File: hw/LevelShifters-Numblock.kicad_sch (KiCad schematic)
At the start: 6 parts, among them U2100 SN74LVCH16T245, U2101 SN74LVCH16T245

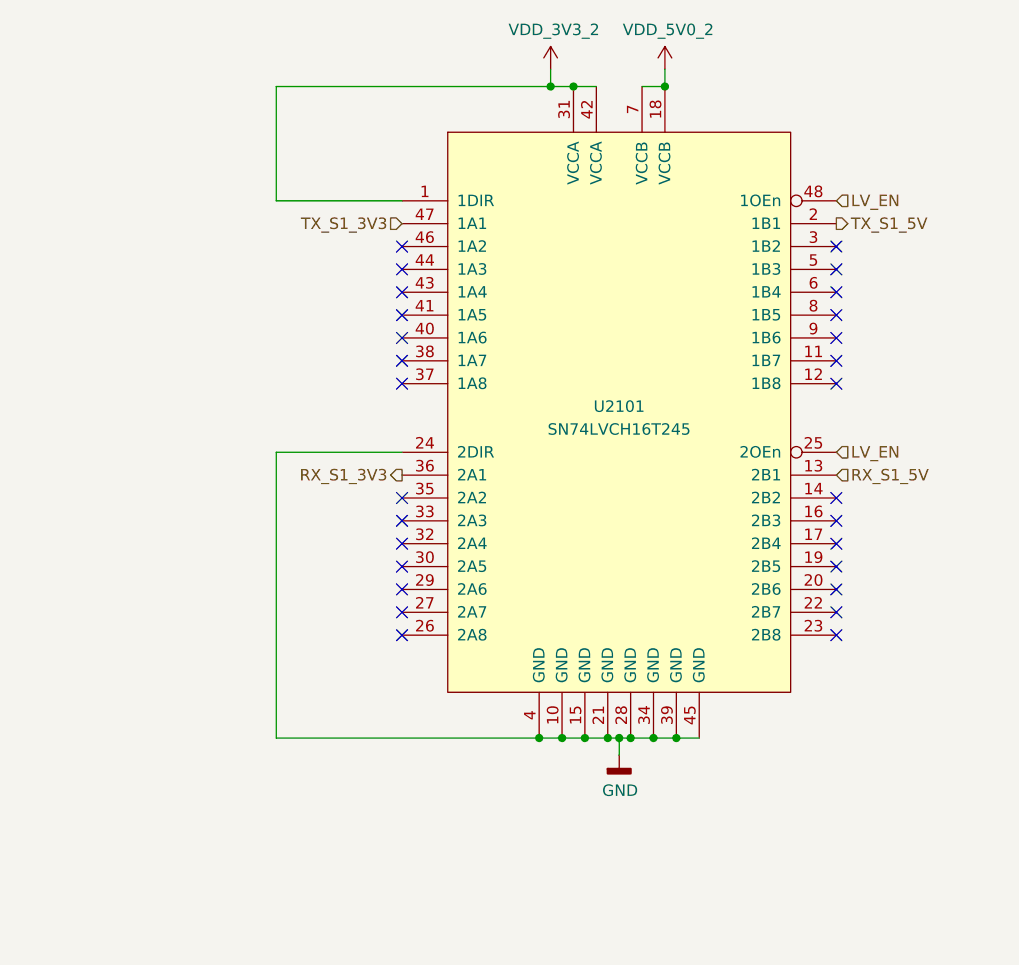
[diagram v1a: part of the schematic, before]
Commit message: Update schematic:
- Add ESD protection.
- Adjust distance bolts so they fit to the MX mounting plate.
- Make key layout symmetric.
- Add resistor to TX driver outputs.
- Use alternate IO functions on inter-board connectors.
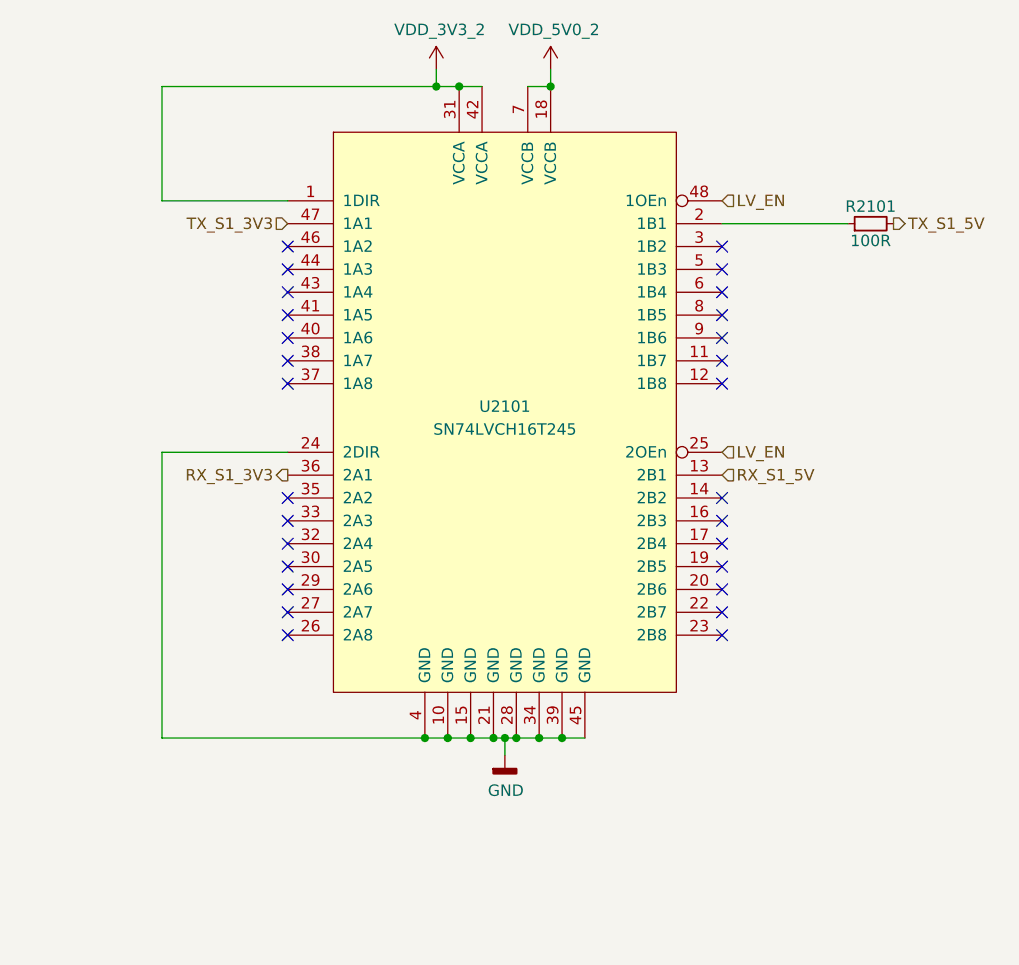
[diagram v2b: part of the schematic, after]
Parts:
- added R2101: 100R, Keyboard:R_0402, symbol Keyboard:100R
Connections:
- net TX_S1_5V: now also R2101.2; no longer U2101.2 (1B1)
- new net: R2101.1, U2101.2 (1B1)
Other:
- moved on the sheet: U2101

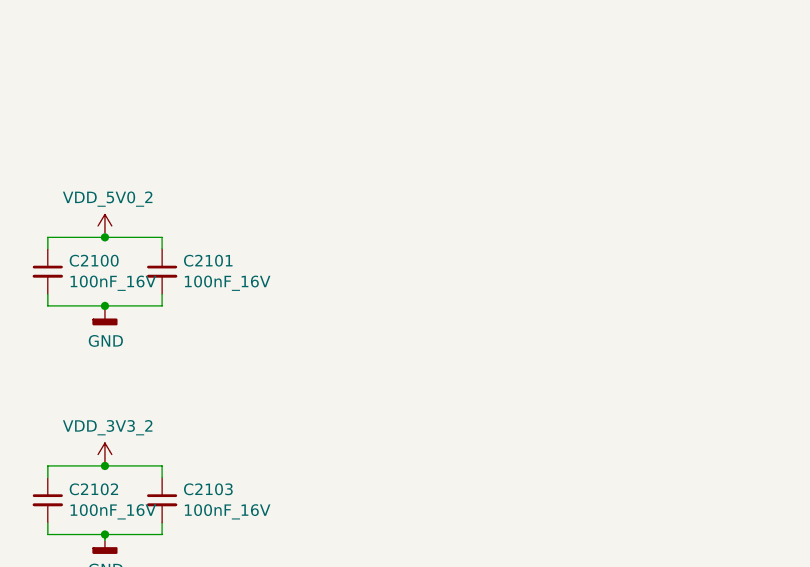
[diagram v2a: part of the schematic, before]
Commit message: Add current probes to 3.3V and pull-up to LV_EN.
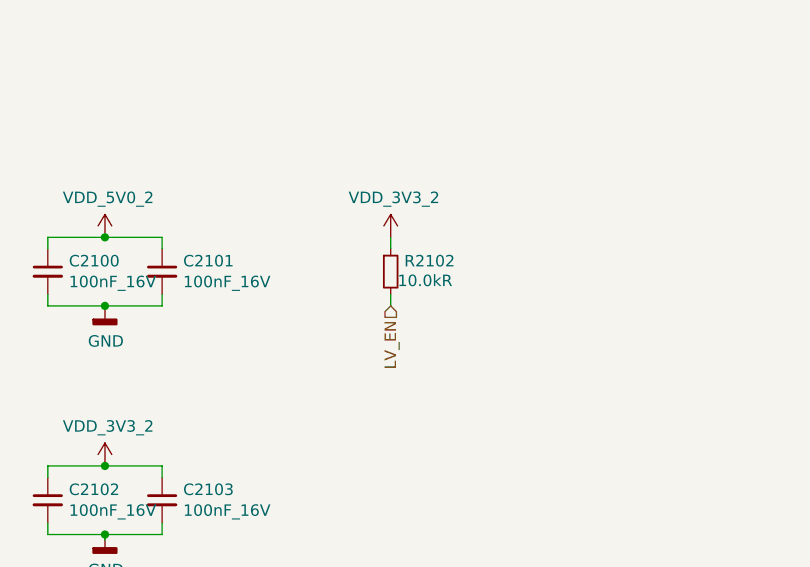
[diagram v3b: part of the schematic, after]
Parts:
- added R2102: 10.0kR, Keyboard:R_0402, symbol Keyboard:10.0kR
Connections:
- net LV_EN: now also R2102.2
- net VDD_3V3_2: now also R2102.1
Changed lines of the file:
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@@
+    (stroke (width 0) (type default) (color 0 0 0 0))
+  )
+  (wire (pts (xy 76.2 140.97) (xy 76.2 139.7))
     (stroke (width 0) (type default) (color 0 0 0 0))
   )
@@
   )
   (wire (pts (xy 214.63 24.765) (xy 214.63 26.67))
+    (stroke (width 0) (type default) (color 0 0 0 0))
+  )
+  (wire (pts (xy 76.2 146.05) (xy 76.2 147.32))
     (stroke (width 0) (type default) (color 0 0 0 0))
   )
@@
   )
   (hierarchical_label "LR7_3V3" (shape input) (at 33.02 57.15 180)
+    (effects (font (size 1.27 1.27)) (justify right))
+  )
+  (hierarchical_label "LV_EN" (shape input) (at 76.2 147.32 270)
     (effects (font (size 1.27 1.27)) (justify right))
   )
@@
     (pin "2")
   )
+  (symbol (lib_id "Keyboard:10.0kR") (at 76.2 143.51 0) (unit 1)
+    (in_bom yes) (on_board yes)
+    (property "Reference" "R2102" (id 0) (at 77.6986 142.3416 0)
+      (effects (font (size 1.27 1.27)) (justify left))
+    )
+    (property "Value" "10.0kR" (id 1) (at 76.962 144.526 0)
+      (effects (font (size 1.27 1.27)) (justify left))
+    )
+    (property "Footprint" "Keyboard:R_0402" (id 2) (at 74.422 145.542 0)
+      (effects (font (size 1.27 1.27)) hide)
+    )
+    (property "Datasheet" "667-ERJ-2RKF1002X" (id 3) (at 76.962 143.002 0)
+      (effects (font (size 1.27 1.27)) hide)
+    )
+    (property "mouser#" "667-ERJ-2RKF1002X" (id 4) (at 79.502 140.462 0)
+      (effects (font (size 1.524 1.524)) hide)
+    )
+    (pin "1")
+    (pin "2")
+  )
+  (symbol (lib_id "Keyboard:VDD_3V3_2") (at 76.2 139.7 0) (unit 1)
+    (in_bom yes) (on_board yes)
+    (property "Reference" "#PWR02111" (id 0) (at 76.2 143.51 0)
+      (effects (font (size 1.27 1.27)) hide)
+    )
+    (property "Value" "VDD_3V3_2" (id 1) (at 76.581 135.3058 0))
+    (property "Footprint" "" (id 2) (at 76.2 139.7 0)
+      (effects (font (size 1.27 1.27)) hide)
+    )
+    (property "Datasheet" "" (id 3) (at 76.2 139.7 0)
+      (effects (font (size 1.27 1.27)) hide)
+    )
+    (pin "1")
+  )
 )
